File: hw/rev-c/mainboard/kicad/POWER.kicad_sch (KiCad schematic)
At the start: 64 parts, among them J10 5V PWR, J11 9V POWER, J13 9V POWER, J8 PET POWER, U3 AMS1117-3.3, U4 LM317AG-TN3-R, U5 LM317AG-TN3-R, U6 TPS5430DDA

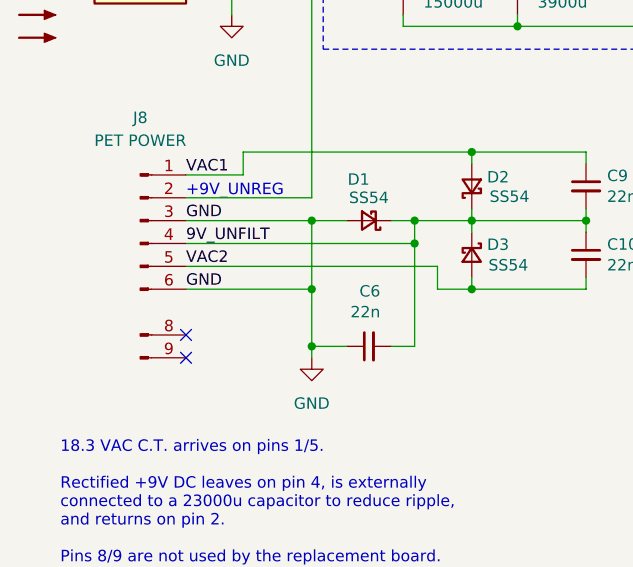
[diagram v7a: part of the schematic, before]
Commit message: hw: remove extra gnd pin on pet power connector
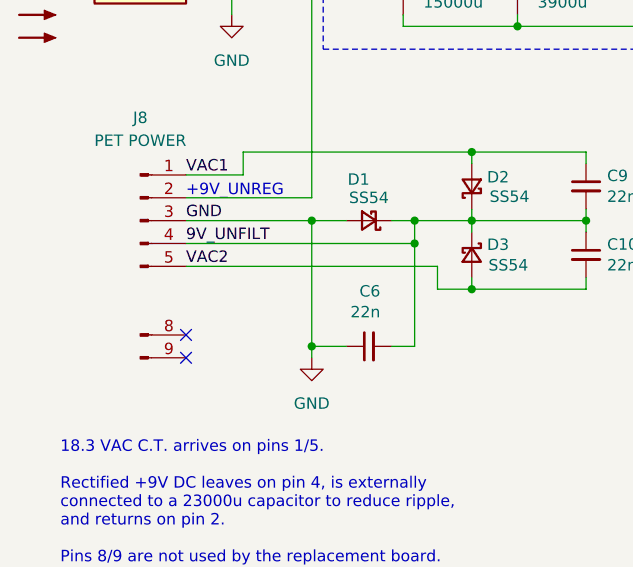
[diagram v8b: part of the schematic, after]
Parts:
- C7: footprint Capacitor_THT:CP_Radial_D12.5mm_P5.00mm -> Capacitor_THT:CP_Radial_D16.0mm_P7.50mm
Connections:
- net GND: no longer J8.6 (GND)
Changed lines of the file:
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@@
 	)
 	(junction
-		(at 49.53 74.93)
-		(diameter 0)
-		(color 0 0 0 0)
-	)
-	(junction
 		(at 49.53 81.28)
 		(diameter 0)
@@
 	(wire
 		(pts
-			(xy 35.56 74.93) (xy 49.53 74.93)
-		)
-		(stroke
-			(width 0)
-			(type default)
-		)
-	)
-	(wire
-		(pts
 			(xy 128.27 87.63) (xy 137.16 87.63)
 		)
@@
 	(wire
 		(pts
-			(xy 49.53 67.31) (xy 49.53 74.93)
-		)
-		(stroke
-			(width 0)
-			(type default)
-		)
-	)
-	(wire
-		(pts
 			(xy 152.4 24.13) (xy 152.4 25.4)
 		)
@@
 	(wire
 		(pts
-			(xy 49.53 74.93) (xy 49.53 81.28)
+			(xy 49.53 67.31) (xy 49.53 81.28)
 		)
 		(stroke
@@
 		)
 	)
-	(label "GND"
-		(at 35.56 74.93 0)
-		(fields_autoplaced yes)
-		(effects
-			(font
-				(size 1.27 1.27)
-			)
-			(justify left bottom)
-		)
-	)
 	(label "VAC1"
 		(at 35.56 62.23 0)
@@
 			)
 		)
-		(property "Footprint" "Capacitor_THT:CP_Radial_D12.5mm_P5.00mm"
+		(property "Footprint" "Capacitor_THT:CP_Radial_D16.0mm_P7.50mm"
 			(at 72.39 41.91 0)
 			(effects
@@
 		(pin "5"
 		)
-		(pin "6"
-		)
 		(pin "8"
